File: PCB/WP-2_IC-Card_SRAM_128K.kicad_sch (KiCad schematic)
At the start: 10 parts, among them J1 SMS-138-01-G-S, U1 628128_TSOP

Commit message: file names, page titles, mram relocate parts
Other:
- title: WP-2_IC-Card_RAM_128K -> WP-2_IC-Card_SRAM_128K
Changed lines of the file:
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@@
 	(paper "USLetter")
 	(title_block
-		(title "WP-2_IC-Card_RAM_128K")
-		(date "2023-12-12")
-		(rev "012")
+		(title "WP-2_IC-Card_SRAM_128K")
+		(date "2024-08-22")
+		(rev "013")
 		(company "Brian K. White - b.kenyon.w@gmail.com")
 	)

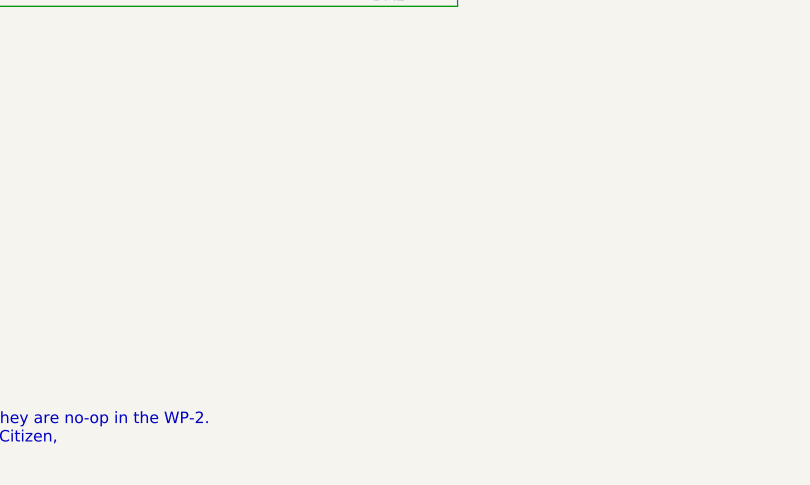
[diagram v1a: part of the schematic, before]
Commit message: local symbol & footprint library organization, add shielded mram version
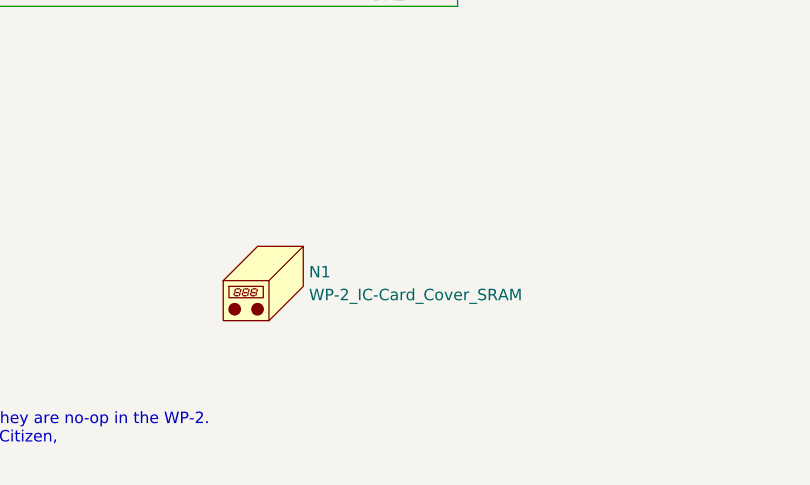
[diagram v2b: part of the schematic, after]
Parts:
- added N1: WP-2_IC-Card_Cover_SRAM, 000_LOCAL:WP-2_IC_Card_Cover_RAM, symbol 000_LOCAL:Housing
- BT1: footprint 0_LOCAL:2016_battery_holder_smt -> 000_LOCAL:2016_battery_holder_smt
- C1, C2, C3, C4: footprint 0_LOCAL:C_0805_1mm -> 000_LOCAL:C_0805_1mm; symbol 0_LOCAL:C_Small -> 000_LOCAL:C_Small
- DA1: footprint 0_LOCAL:SOT-23 -> 000_LOCAL:SOT-23; symbol 0_LOCAL:BAV170 -> 000_LOCAL:BAV170
- J1: footprint 0_LOCAL:SMS-138-01-x-x_edge -> 000_LOCAL:SMS-138-01-x-x_pcb_edge; symbol 0_LOCAL:Conn_01x38_Female -> 000_LOCAL:Conn_01x38_Female
- R1, R2: footprint 0_LOCAL:R_0805 -> 000_LOCAL:R_0805; symbol 0_LOCAL:R -> 000_LOCAL:R
- U1: footprint 0_LOCAL:TSOP32-dual -> 000_LOCAL:TSOP32-dual; symbol 0_LOCAL:62-65C1024_TSOP-I-32 -> 000_LOCAL:62-65C1024_TSOP-I-32
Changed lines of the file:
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@@
 	)
 	(symbol
-		(lib_id "0_LOCAL:Conn_01x38_Female")
+		(lib_id "000_LOCAL:Conn_01x38_Female")
 		(at 83.82 99.06 0)
 		(mirror y)
@@
 			)
 		)
-		(property "Footprint" "0_LOCAL:SMS-138-01-x-x_edge"
+		(property "Footprint" "000_LOCAL:SMS-138-01-x-x_pcb_edge"
 			(at 83.82 99.06 0)
 			(effects
@@
 			)
 		)
-		(property "Footprint" "0_LOCAL:2016_battery_holder_smt"
+		(property "Footprint" "000_LOCAL:2016_battery_holder_smt"
 			(at 128.524 139.7 90)
 			(effects
@@
 	)
 	(symbol
-		(lib_id "0_LOCAL:R")
+		(lib_id "000_LOCAL:R")
 		(at 163.83 109.22 90)
 		(mirror x)
@@
 			)
 		)
-		(property "Footprint" "0_LOCAL:R_0805"
+		(property "Footprint" "000_LOCAL:R_0805"
 			(at 163.83 107.442 90)
 			(effects
@@
 	)
 	(symbol
-		(lib_id "0_LOCAL:C_Small")
+		(lib_id "000_LOCAL:C_Small")
 		(at 120.65 120.65 0)
 		(mirror y)
@@
 			)
 		)
-		(property "Footprint" "0_LOCAL:C_0805_1mm"
+		(property "Footprint" "000_LOCAL:C_0805_1mm"
 			(at 120.65 120.65 0)
 			(effects
@@
 	)
 	(symbol
-		(lib_id "0_LOCAL:C_Small")
+		(lib_id "000_LOCAL:C_Small")
 		(at 186.69 53.34 270)
 		(mirror x)
@@
 			)
 		)
-		(property "Footprint" "0_LOCAL:C_0805_1mm"
+		(property "Footprint" "000_LOCAL:C_0805_1mm"
 			(at 186.69 53.34 0)
 			(effects
@@
 	)
 	(symbol
-		(lib_id "0_LOCAL:R")
+		(lib_id "000_LOCAL:R")
 		(at 134.62 118.11 90)
 		(mirror x)
@@
 			)
 		)
-		(property "Footprint" "0_LOCAL:R_0805"
+		(property "Footprint" "000_LOCAL:R_0805"
 			(at 134.62 116.332 90)
 			(effects
@@
 	)
 	(symbol
-		(lib_id "0_LOCAL:C_Small")
+		(lib_id "000_LOCAL:C_Small")
 		(at 128.27 120.65 0)
 		(mirror y)
@@
 			)
 		)
-		(property "Footprint" "0_LOCAL:C_0805_1mm"
+		(property "Footprint" "000_LOCAL:C_0805_1mm"
 			(at 128.27 120.65 0)
 			(effects
@@
 	)
 	(symbol
+		(lib_id "000_LOCAL:Housing")
+		(at 127 177.8 0)
+		(unit 1)
+		(exclude_from_sim yes)
+		(in_bom yes)
+		(on_board yes)
+		(dnp no)
+		(fields_autoplaced yes)
+		(property "Reference" "N1"
+			(at 130.81 176.8474 0)
+			(effects
+				(font
+					(size 1.27 1.27)
+				)
+				(justify left)
+			)
+		)
+		(property "Value" "WP-2_IC-Card_Cover_SRAM"
+			(at 130.81 179.3874 0)
+			(effects
+				(font
+					(size 1.27 1.27)
+				)
+				(justify left)
+			)
+		)
+		(property "Footprint" "000_LOCAL:WP-2_IC_Card_Cover_RAM"
+			(at 128.27 176.53 0)
+			(effects
+				(font
+					(size 1.27 1.27)
+				)
+				(hide yes)
+			)
+		)
+		(property "Datasheet" "~"
+			(at 128.27 176.53 0)
+			(effects
+				(font
+					(size 1.27 1.27)
+				)
+				(hide yes)
+			)
+		)
+		(property "Description" "Housing"
+			(at 127 177.8 0)
+			(effects
+				(font
+					(size 1.27 1.27)
+				)
+				(hide yes)
+			)
+		)
+		(instances
+			(project ""
+				(path "/61a4a6ea-f14c-4701-87bd-6399392c074d"
+					(reference "N1")
+					(unit 1)
+				)
+			)
+		)
+	)
+	(symbol
 		(lib_id "power:GND")
 		(at 177.8 106.68 270)
@@
 	)
 	(symbol
-		(lib_id "0_LOCAL:BAV170")
+		(lib_id "000_LOCAL:BAV170")
 		(at 139.7 139.7 0)
 		(mirror x)
@@
 			)
 		)
-		(property "Footprint" "0_LOCAL:SOT-23"
+		(property "Footprint" "000_LOCAL:SOT-23"
 			(at 139.7 139.7 0)
 			(effects
@@
 	)
 	(symbol
-		(lib_id "0_LOCAL:C_Small")
+		(lib_id "000_LOCAL:C_Small")
 		(at 124.46 120.65 0)
 		(mirror y)
@@
 			)
 		)
-		(property "Footprint" "0_LOCAL:C_0805_1mm"
+		(property "Footprint" "000_LOCAL:C_0805_1mm"
 			(at 124.46 120.65 0)
 			(effects
@@
 	)
 	(symbol
-		(lib_id "0_LOCAL:62-65C1024_TSOP-I-32")
+		(lib_id "000_LOCAL:62-65C1024_TSOP-I-32")
 		(at 193.04 88.9 0)
 		(unit 1)
@@
 			)
 		)
-		(property "Footprint" "0_LOCAL:TSOP32-dual"
+		(property "Footprint" "000_LOCAL:TSOP32-dual"
 			(at 193.04 91.44 0)
 			(effects

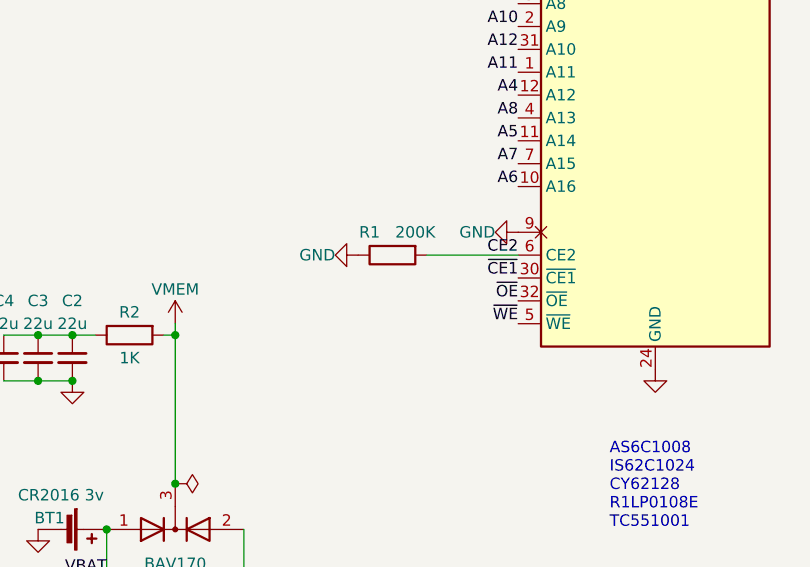
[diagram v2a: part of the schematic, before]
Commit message: cleanup names, cover inside corner reliefs
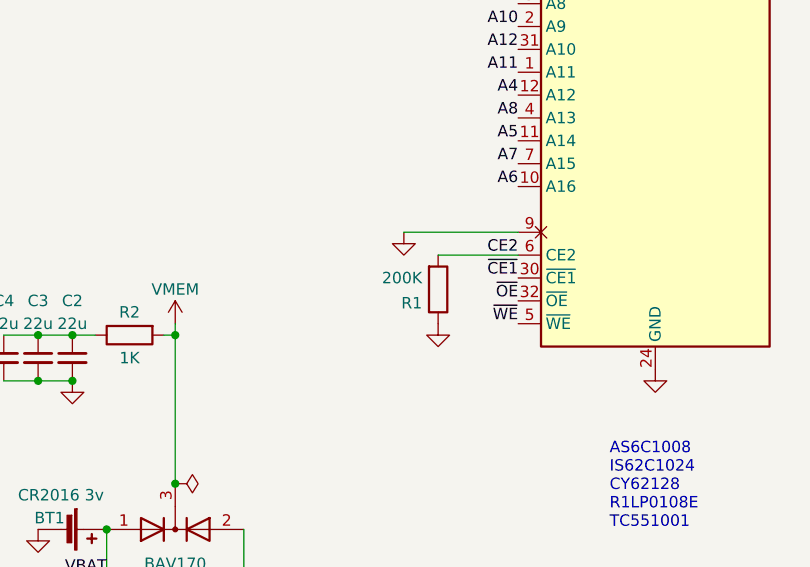
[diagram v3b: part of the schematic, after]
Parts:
- N1: footprint 000_LOCAL:WP-2_IC_Card_Cover_RAM -> 000_LOCAL:WP-2_IC-Card_Cover_SRAM; now left out of the parts list
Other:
- moved on the sheet: R1
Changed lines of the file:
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@@
+	(wire
+		(pts
+			(xy 168.91 109.22) (xy 177.8 109.22)
+		)
+		(stroke
+			(width 0)
+			(type default)
+		)
+	)
 	(wire
 		(pts
@@
 	(wire
 		(pts
-			(xy 193.04 53.34) (xy 193.04 55.88)
+			(xy 165.1 106.68) (xy 177.8 106.68)
 		)
 		(stroke
@@
 	(wire
 		(pts
-			(xy 128.27 118.11) (xy 130.81 118.11)
+			(xy 193.04 53.34) (xy 193.04 55.88)
 		)
 		(stroke
@@
 	(wire
 		(pts
-			(xy 189.23 53.34) (xy 193.04 53.34)
+			(xy 128.27 118.11) (xy 130.81 118.11)
 		)
 		(stroke
@@
 	(wire
 		(pts
-			(xy 95.25 55.88) (xy 88.9 55.88)
+			(xy 189.23 53.34) (xy 193.04 53.34)
 		)
 		(stroke
@@
 	(wire
 		(pts
-			(xy 132.08 144.78) (xy 132.08 139.7)
+			(xy 95.25 55.88) (xy 88.9 55.88)
 		)
 		(stroke
@@
 	(wire
 		(pts
-			(xy 88.9 147.32) (xy 147.32 147.32)
+			(xy 132.08 144.78) (xy 132.08 139.7)
 		)
 		(stroke
@@
 	(wire
 		(pts
-			(xy 120.65 118.11) (xy 124.46 118.11)
+			(xy 88.9 147.32) (xy 147.32 147.32)
 		)
 		(stroke
@@
 	(wire
 		(pts
-			(xy 95.25 53.34) (xy 101.6 53.34)
+			(xy 120.65 118.11) (xy 124.46 118.11)
 		)
 		(stroke
@@
 	(wire
 		(pts
-			(xy 124.46 118.11) (xy 128.27 118.11)
+			(xy 95.25 53.34) (xy 101.6 53.34)
 		)
 		(stroke
@@
 	(wire
 		(pts
-			(xy 95.25 53.34) (xy 88.9 53.34)
+			(xy 124.46 118.11) (xy 128.27 118.11)
 		)
 		(stroke
@@
 	(wire
 		(pts
-			(xy 139.7 118.11) (xy 139.7 116.84)
+			(xy 95.25 53.34) (xy 88.9 53.34)
 		)
 		(stroke
@@
 	(wire
 		(pts
-			(xy 139.7 118.11) (xy 139.7 134.62)
+			(xy 139.7 118.11) (xy 139.7 116.84)
 		)
 		(stroke
@@
 	(wire
 		(pts
-			(xy 88.9 144.78) (xy 132.08 144.78)
+			(xy 139.7 118.11) (xy 139.7 134.62)
 		)
 		(stroke
@@
 	(wire
 		(pts
-			(xy 167.64 109.22) (xy 177.8 109.22)
+			(xy 88.9 144.78) (xy 132.08 144.78)
 		)
 		(stroke
@@
 	(symbol
 		(lib_id "000_LOCAL:R")
-		(at 163.83 109.22 90)
+		(at 168.91 113.03 0)
 		(mirror x)
 		(unit 1)
@@
 		(dnp no)
 		(property "Reference" "R1"
-			(at 161.29 106.68 90)
-			(effects
-				(font
-					(size 1.27 1.27)
-				)
+			(at 167.132 114.554 0)
+			(effects
+				(font
+					(size 1.27 1.27)
+				)
+				(justify right)
 			)
 		)
 		(property "Value" "200K"
-			(at 166.37 106.68 90)
-			(effects
-				(font
-					(size 1.27 1.27)
-				)
+			(at 167.132 111.76 0)
+			(effects
+				(font
+					(size 1.27 1.27)
+				)
+				(justify right)
 			)
 		)
 		(property "Footprint" "000_LOCAL:R_0805"
-			(at 163.83 107.442 90)
+			(at 167.132 113.03 90)
 			(effects
 				(font
@@
 		)
 		(property "Datasheet" "~"
-			(at 163.83 109.22 0)
+			(at 168.91 113.03 0)
 			(effects
 				(font
@@
 		)
 		(property "Description" "RES SMD 200K OHM 1% 1/8W 0805"
-			(at 163.83 109.22 0)
+			(at 168.91 113.03 0)
 			(effects
 				(font
@@
 		)
 		(property "MPN" "CRCW0805200KFKEA"
-			(at 163.83 109.22 90)
+			(at 168.91 113.03 90)
 			(effects
 				(font
@@
 	)
 	(symbol
+		(lib_id "power:GND")
+		(at 165.1 106.68 0)
+		(unit 1)
+		(exclude_from_sim no)
+		(in_bom yes)
+		(on_board yes)
+		(dnp no)
+		(property "Reference" "#PWR05"
+			(at 165.1 113.03 0)
+			(effects
+				(font
+					(size 1.27 1.27)
+				)
+				(hide yes)
+			)
+		)
+		(property "Value" "GND"
+			(at 165.1 110.49 0)
+			(effects
+				(font
+					(size 1.27 1.27)
+				)
+				(hide yes)
+			)
+		)
+		(property "Footprint" ""
+			(at 165.1 106.68 0)
+			(effects
+				(font
+					(size 1.27 1.27)
+				)
+				(hide yes)
+			)
+		)
+		(property "Datasheet" ""
+			(at 165.1 106.68 0)
+			(effects
+				(font
+					(size 1.27 1.27)
+				)
+				(hide yes)
+			)
+		)
+		(property "Description" ""
+			(at 165.1 106.68 0)
+			(effects
+				(font
+					(size 1.27 1.27)
+				)
+				(hide yes)
+			)
+		)
+		(pin "1"
+		)
+		(instances
+			(project "WP-2_IC-Card_SRAM_128K"
+				(path "/61a4a6ea-f14c-4701-87bd-6399392c074d"
+					(reference "#PWR05")
+					(unit 1)
+				)
+			)
+		)
+	)
+	(symbol
 		(lib_id "000_LOCAL:Housing")
 		(at 127 177.8 0)
 		(unit 1)
 		(exclude_from_sim yes)
-		(in_bom yes)
+		(in_bom no)
 		(on_board yes)
 		(dnp no)
@@
 			)
 		)
-		(property "Footprint" "000_LOCAL:WP-2_IC_Card_Cover_RAM"
+		(property "Footprint" "000_LOCAL:WP-2_IC-Card_Cover_SRAM"
 			(at 128.27 176.53 0)
 			(effects
@@
 	(symbol
 		(lib_id "power:GND")
-		(at 177.8 106.68 270)
+		(at 168.91 116.84 0)
 		(unit 1)
 		(exclude_from_sim no)
@@
 		(on_board yes)
 		(dnp no)
-		(property "Reference" "#PWR0103"
-			(at 171.45 106.68 0)
+		(property "Reference" "#PWR04"
+			(at 168.91 123.19 0)
 			(effects
 				(font
@@
 		)
 		(property "Value" "GND"
-			(at 175.26 106.68 90)
-			(effects
-				(font
-					(size 1.27 1.27)
-				)
-				(justify right)
+			(at 168.91 120.65 0)
+			(effects
+				(font
+					(size 1.27 1.27)
+				)
+				(hide yes)
 			)
 		)
 		(property "Footprint" ""
-			(at 177.8 106.68 0)
+			(at 168.91 116.84 0)
 			(effects
 				(font
@@
 		)
 		(property "Datasheet" ""
-			(at 177.8 106.68 0)
+			(at 168.91 116.84 0)
 			(effects
 				(font
@@
 		)
 		(property "Description" ""
-			(at 177.8 106.68 0)
+			(at 168.91 116.84 0)
 			(effects
 				(font
@@
 		)
 		(instances
-			(project "WP-2_IC-Card_RAM"
+			(project "WP-2_IC-Card_SRAM_128K"
 				(path "/61a4a6ea-f14c-4701-87bd-6399392c074d"
-					(reference "#PWR0103")
+					(reference "#PWR04")
 					(unit 1)
 				)
@@
 					(unit 1)
 				)
-			)
-		)
-	)
-	(symbol
-		(lib_id "power:GND")
-		(at 160.02 109.22 270)
-		(unit 1)
-		(exclude_from_sim no)
-		(in_bom yes)
-		(on_board yes)
-		(dnp no)
-		(property "Reference" "#PWR0109"
-			(at 153.67 109.22 0)
-			(effects
-				(font
-					(size 1.27 1.27)
-				)
-				(hide yes)
-			)
-		)
-		(property "Value" "GND"
-			(at 157.48 109.22 90)
-			(effects
-				(font
-					(size 1.27 1.27)
-				)
-				(justify right)
-			)
-		)
-		(property "Footprint" ""
-			(at 160.02 109.22 0)
-			(effects
-				(font
-					(size 1.27 1.27)
-				)
-				(hide yes)
-			)
-		)
-		(property "Datasheet" ""
-			(at 160.02 109.22 0)
-			(effects
-				(font
-					(size 1.27 1.27)
-				)
-				(hide yes)
-			)
-		)
-		(property "Description" ""
-			(at 160.02 109.22 0)
-			(effects
-				(font
-					(size 1.27 1.27)
-				)
-				(hide yes)
-			)
-		)
-		(pin "1"
-		)
-		(instances
-			(project "WP-2_IC-Card_RAM"
-				(path "/61a4a6ea-f14c-4701-87bd-6399392c074d"
-					(reference "#PWR0109")
-					(unit 1)
-				)

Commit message: rom wren sw, boms, footprints, shielded mram
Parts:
- removed C4: 22u, 000_LOCAL:C_0805_1mm, symbol 000_LOCAL:C_Small
- removed R2: 1K, 000_LOCAL:R_0805, symbol 000_LOCAL:R
- BT1: value CR2016 3v -> CR2016
- C1: footprint 000_LOCAL:C_0805_1mm -> 000_LOCAL:C_0805
- C2, C3: footprint 000_LOCAL:C_0805_1mm -> 000_LOCAL:C_1206; MPN CL21A226MOCLRNC -> CL31A226MOCLNNC
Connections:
- net VMEM: now also C2.1, C3.1
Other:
- moved on the sheet: C2
